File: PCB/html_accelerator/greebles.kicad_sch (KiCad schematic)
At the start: 16 parts, among them U12 MCS9990

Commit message: layout and 3d updates
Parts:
- removed RN1 (x2): 1k, Resistor_SMD:R_Array_Convex_4x1206, symbol Device:R_Pack04
- added MECH1, MECH2: ~, html_accel_footprints:Heatsink, symbol html_accel_Symbols:Heatsink
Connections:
- net GND: now also U12.1 (GND1), U12.10 (PCIE_RXDP), U12.100 (USB0_PWR_EN_N), U12.101 (LN_STAT2), U12.102 (USB1_OVCI_N), U12.103 (USB1_PWR_EN_N), U12.104 (LN_STAT0), U12.105 (LN_STAT1), U12.106 (+3.3VIO), U12.107 (GND20), U12.108 (GND21), U12.109 (+1.2V), U12.11 (GND3), U12.110 (+3.3VA), U12.111 (+3.3VA), U12.112 (USB2_DM), U12.113 (USB2_DP), U12.114 (GND22), U12.115 (GND23), U12.116 (USB2_IBERF), U12.117 (USB2_OTG_VBUS), U12.118 (GND24), U12.119 (+3.3VA), U12.12 (+1.2VA), U12.120 (GND25), U12.121 (+1.2V), U12.122 (USB2_OVCI_N), U12.123 (USB2_PWR_EN_N), U12.124 (USB2_OTG_ID), U12.125 (USB3_OVCI_N), U12.126 (USB3_PWR_EN_N), U12.127 (+3.3VIO), U12.128 (GND26), U12.13 (PCIE_TXDP), U12.14 (PCIE_TXDN), U12.15 (+1.2VA), U12.16 (+3.3VA_PLL), U12.17 (GND4), U12.18 (GND5), U12.19 (+3.3VA_AUX), U12.2 (+3.3VIN_REG), U12.20 (+1.2V), U12.21 (GND6), U12.22 (PCIE_CLKREQ_N), U12.23 (PCIE_WAKE_N), U12.24 (MODE_SEL0), U12.25 (+3.3VIO), U12.26 (GND7), U12.27 (OTG_EN_N), U12.28 (PCIE_PERST_N), U12.29 (EE_SCL), U12.3 (+1.2VOUT_REG), U12.30 (EE_SDA), U12.31 (SCAN_EN), U12.32 (TEST_EN), U12.33 (+1.2V), U12.34 (GND8), U12.35 (GPIO0/D0), U12.36 (GPIO1/D1), U12.37 (GPIO2/D2), U12.38 (GPIO3/D3), U12.39 (GPIO4/D4), U12.4 (PCIE_REFCLKN), U12.40 (GPIO5/D5), U12.41 (GPIO6/D6), U12.42 (GPIO7/D7), U12.43 (GPIO8/INTA), U12.44 (GPIO9/INTB), U12.45 (GPIO10/INTC), U12.46 (GPIO11/INTD), U12.47 (MODE_SEL1), U12.48 (+3.3VIO), U12.49 (MODE_SEL2), U12.5 (PCIE_REFCLKP), U12.50 (GND9), U12.51 (+3.3VA), U12.52 (+3.3VA), U12.53 (USB3_DM), U12.54 (USB3_DP), U12.55 (GND10), U12.56 (GND11), U12.57 (USB3_IBREF), U12.58 (+1.2V), U12.59 (GND12), U12.6 (+1.2VA_AUX), U12.60 (JTAG_TCK), U12.61 (JTAG_TDI), U12.62 (JTAG_TDO), U12.63 (JTAG_TMS), U12.64 (JTAG_TRST_N), U12.65 (GPIO12/CSA_N), U12.66 (GPIO13/CSB_N), U12.67 (GPIO14/CSC_N), U12.68 (GPIO15/CSD_N), U12.69 (GND13), U12.7 (REXT), U12.70 (+3.3VIO), U12.71 (GPIO16/RESET), U12.72 (GPIO17/IOW_N), U12.73 (GPIO18/IOR_N), U12.74 (GPIO23/IOCHRDY2), U12.75 (GPIO19/A0), U12.76 (GPIO20/A1), U12.77 (GPIO21/A2), U12.78 (GPIO22/IOCHRDY1), U12.79 (GND14), U12.8 (GND2), U12.80 (+1.2V), U12.81 (USB0_XSCI), U12.82 (USB0_XSCO), U12.83 (+3.3VA), U12.84 (+3.3VA), U12.85 (USB0_DM), U12.86 (USB0_DP), U12.87 (GND15), U12.88 (GND16), U12.89 (USB0_IBREF), U12.9 (PCIE_RXDN), U12.90 (+3.3VA), U12.91 (+3.3VA), U12.92 (USB1_DM), U12.93 (USB1_DP), U12.94 (GND17), U12.95 (GND18), U12.96 (USB1_IBREF), U12.97 (GND19), U12.98 (+1.2V), U12.99 (USB0_OVCI_N)
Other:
- moved on the sheet: U12A, U12B, U12C, U12D, U12E

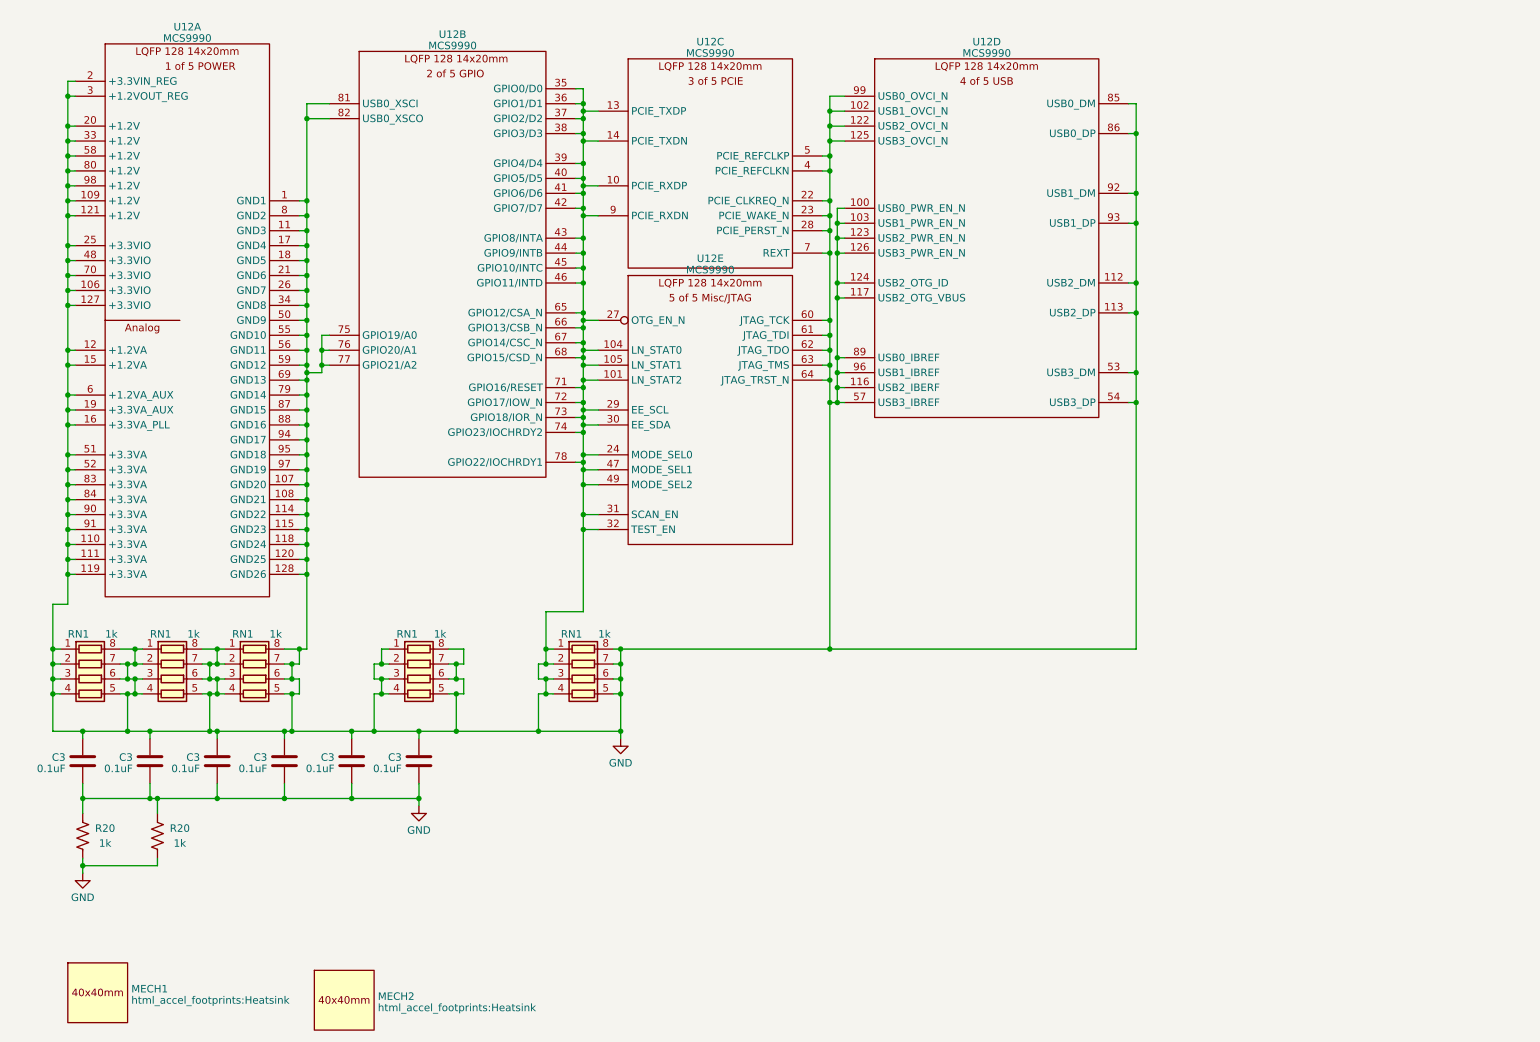
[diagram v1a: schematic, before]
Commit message: constraints for impedance control
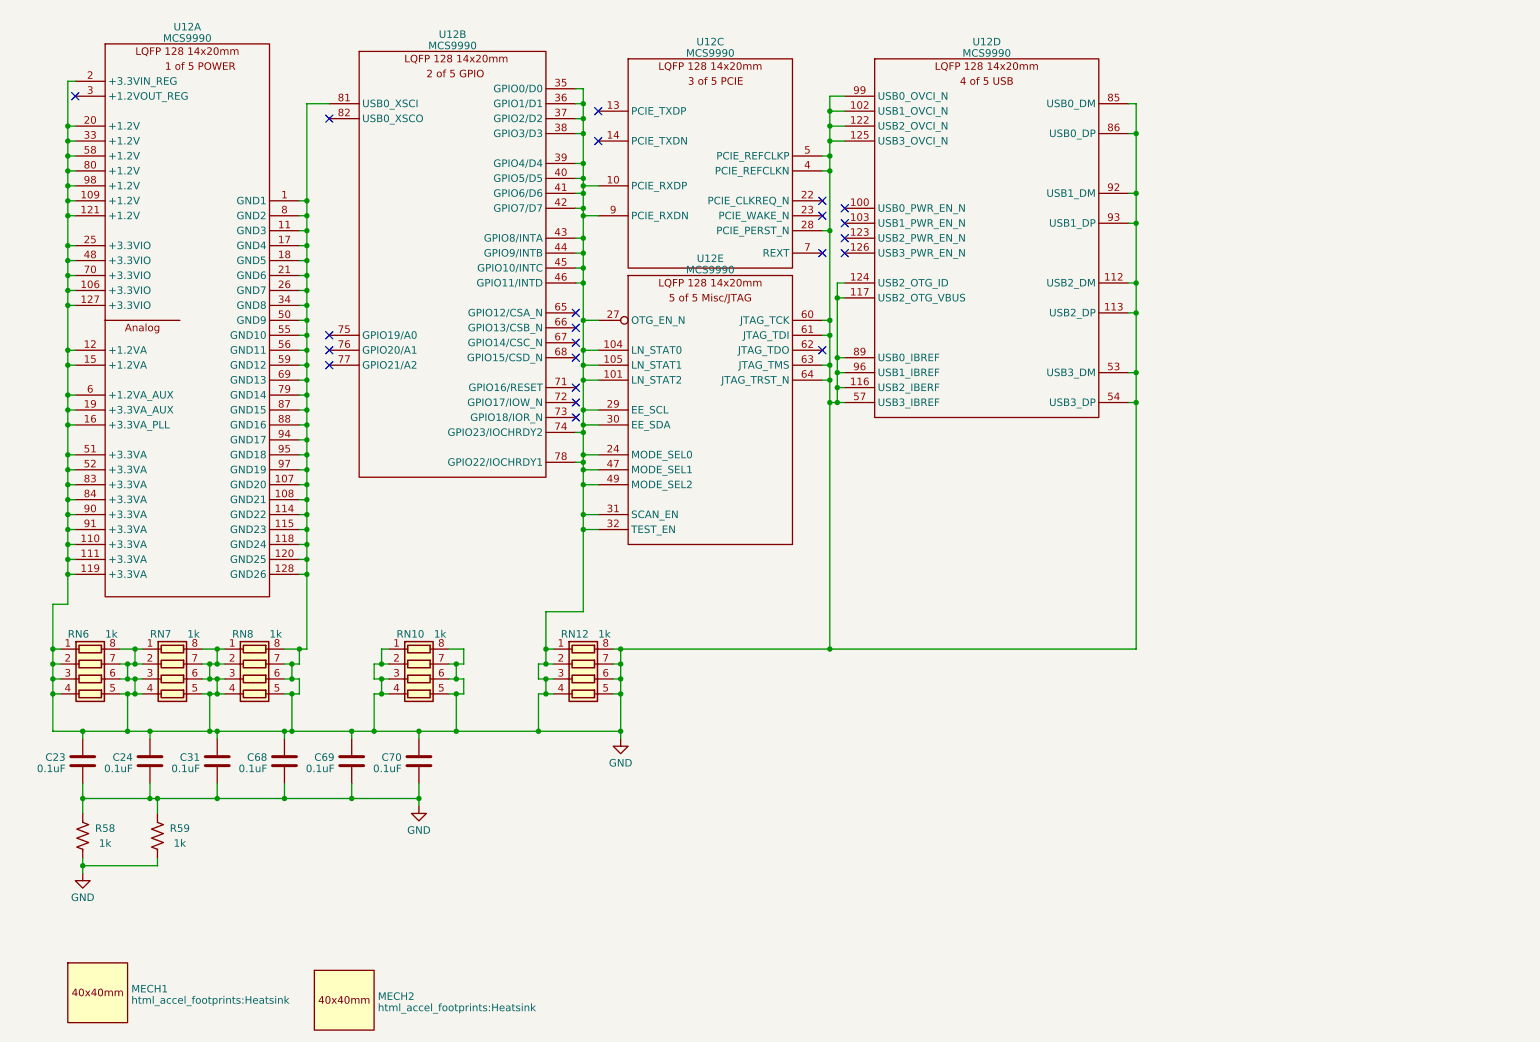
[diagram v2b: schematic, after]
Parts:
- renumbered C3 to C23, C3 to C24, C3 to C31, C3 to C68, C3 to C69, C3 to C70, R20 to R58, R20 to R59, RN1 to RN10, RN1 to RN12, RN1 to RN6, RN1 to RN7, RN1 to RN8
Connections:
- net GND: no longer U12.100 (USB0_PWR_EN_N), U12.103 (USB1_PWR_EN_N), U12.123 (USB2_PWR_EN_N), U12.126 (USB3_PWR_EN_N), U12.13 (PCIE_TXDP), U12.14 (PCIE_TXDN), U12.22 (PCIE_CLKREQ_N), U12.23 (PCIE_WAKE_N), U12.3 (+1.2VOUT_REG), U12.62 (JTAG_TDO), U12.65 (GPIO12/CSA_N), U12.66 (GPIO13/CSB_N), U12.67 (GPIO14/CSC_N), U12.68 (GPIO15/CSD_N), U12.7 (REXT), U12.71 (GPIO16/RESET), U12.72 (GPIO17/IOW_N), U12.73 (GPIO18/IOR_N), U12.75 (GPIO19/A0), U12.76 (GPIO20/A1), U12.77 (GPIO21/A2), U12.82 (USB0_XSCO)
- no-connect marks 0 -> 22

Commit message: Ongoing layout, Update to Kicad V10
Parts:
- MECH1, MECH2: value ~ -> (none)

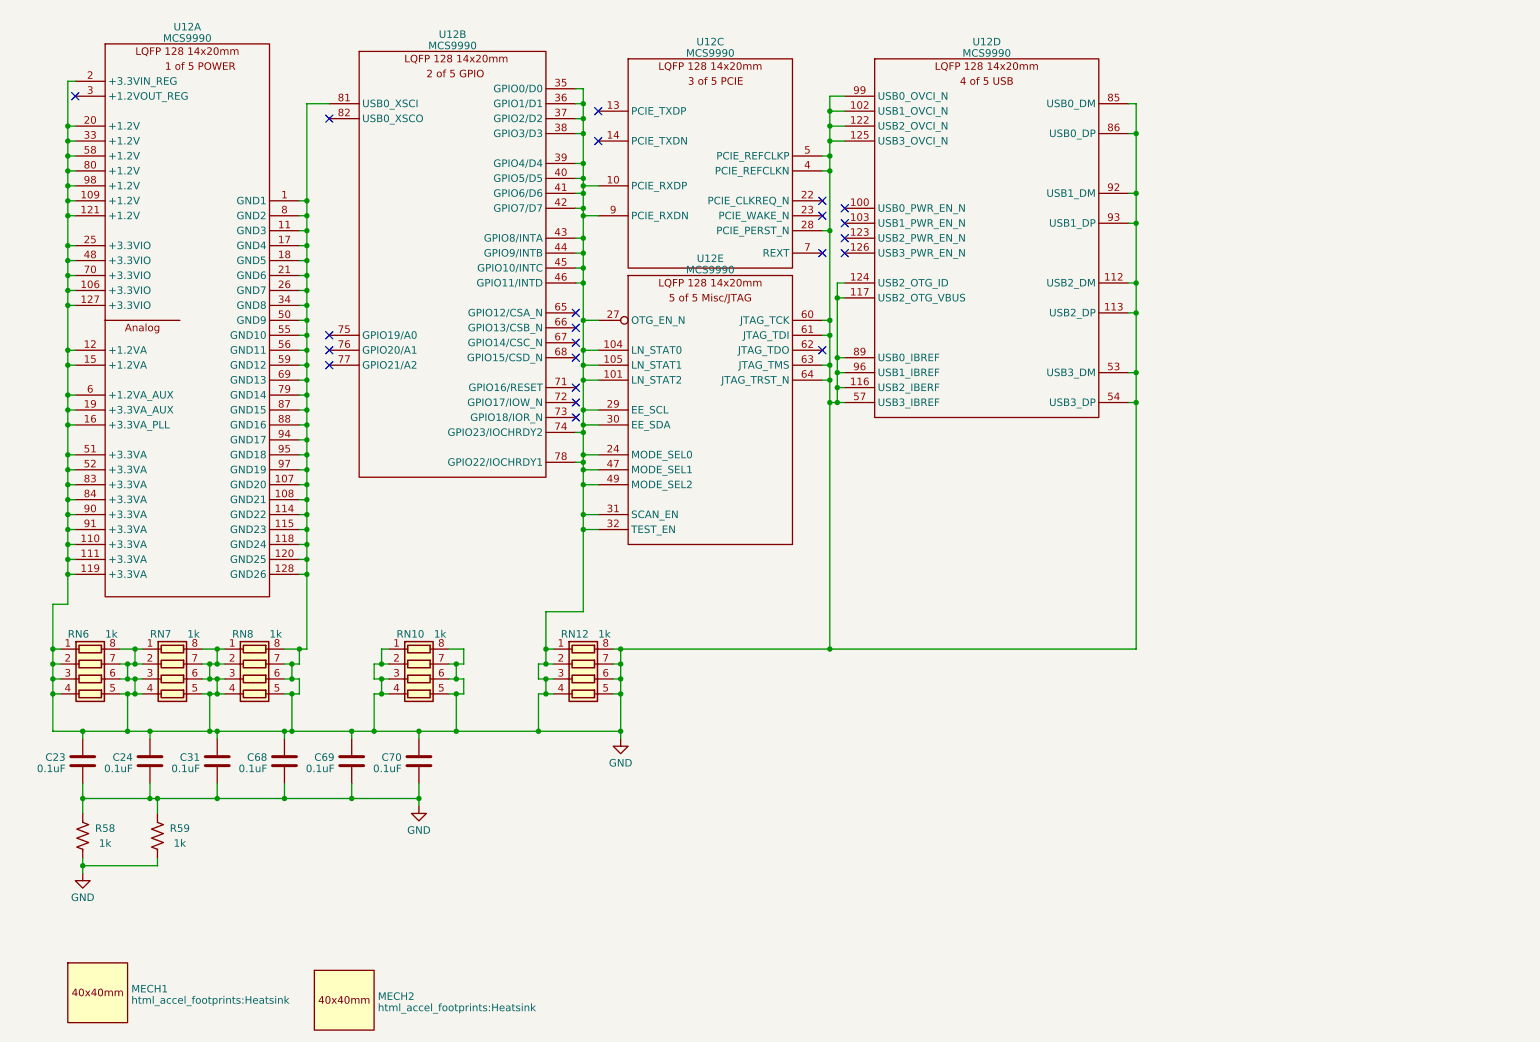
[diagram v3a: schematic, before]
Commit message: Additional routing greebles, cleanup and gerber export with BOM
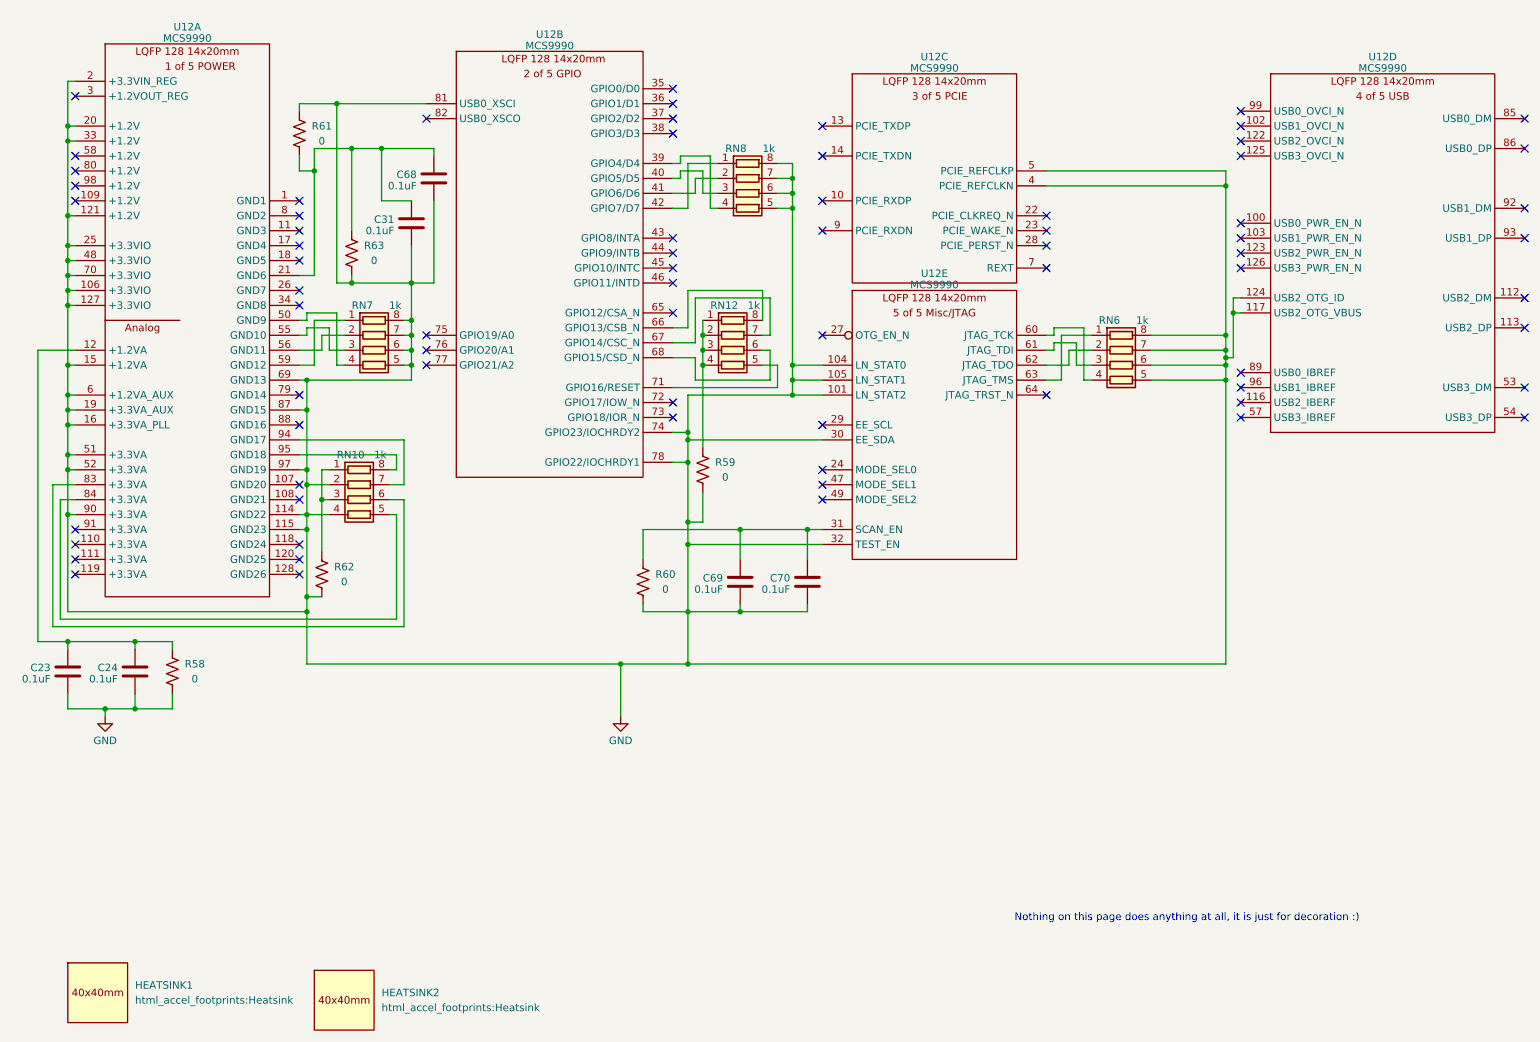
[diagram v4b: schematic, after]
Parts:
- added R60, R61, R62, R63: 0, Resistor_SMD:R_0805_2012Metric_Pad1.20x1.40mm_HandSolder, symbol Device:R_US
- R58, R59: value 1k -> 0
- renumbered MECH1 to HEATSINK1, MECH2 to HEATSINK2
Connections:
- net GND: now also R60.2, R61.1, R62.2, R63.2; no longer C23.2, C24.2, C31.2, C68.2, C69.2, C70.2, R58.1, R59.1, RN10.1 (R1.1), RN10.3 (R3.1), RN10.5 (R4.2), RN10.6 (R3.2), RN10.7 (R2.2), RN10.8 (R1.2), RN12.1 (R1.1), RN12.2 (R2.1), RN12.3 (R3.1), RN12.4 (R4.1), RN12.5 (R4.2), RN12.6 (R3.2), RN12.7 (R2.2), RN12.8 (R1.2), RN6.1 (R1.1), RN6.2 (R2.1), RN6.3 (R3.1), RN6.4 (R4.1), RN7.1 (R1.1), RN7.2 (R2.1), RN7.3 (R3.1), RN7.4 (R4.1), RN8.1 (R1.1), RN8.2 (R2.1), RN8.3 (R3.1), RN8.4 (R4.1), U12.1 (GND1), U12.10 (PCIE_RXDP), U12.102 (USB1_OVCI_N), U12.107 (GND20), U12.108 (GND21), U12.109 (+1.2V), U12.11 (GND3), U12.110 (+3.3VA), U12.111 (+3.3VA), U12.112 (USB2_DM), U12.113 (USB2_DP), U12.116 (USB2_IBERF), U12.118 (GND24), U12.119 (+3.3VA), U12.12 (+1.2VA), U12.120 (GND25), U12.122 (USB2_OVCI_N), U12.125 (USB3_OVCI_N), U12.128 (GND26), U12.17 (GND4), U12.18 (GND5), U12.21 (GND6), U12.24 (MODE_SEL0), U12.26 (GND7), U12.27 (OTG_EN_N), U12.28 (PCIE_PERST_N), U12.29 (EE_SCL), U12.31 (SCAN_EN), U12.34 (GND8), U12.35 (GPIO0/D0), U12.36 (GPIO1/D1), U12.37 (GPIO2/D2), U12.38 (GPIO3/D3), U12.39 (GPIO4/D4), U12.40 (GPIO5/D5), U12.41 (GPIO6/D6), U12.42 (GPIO7/D7), U12.43 (GPIO8/INTA), U12.44 (GPIO9/INTB), U12.45 (GPIO10/INTC), U12.46 (GPIO11/INTD), U12.47 (MODE_SEL1), U12.49 (MODE_SEL2), U12.50 (GND9), U12.53 (USB3_DM), U12.54 (USB3_DP), U12.55 (GND10), U12.56 (GND11), U12.57 (USB3_IBREF), U12.58 (+1.2V), U12.59 (GND12), U12.60 (JTAG_TCK), U12.61 (JTAG_TDI), U12.63 (JTAG_TMS), U12.64 (JTAG_TRST_N), U12.79 (GND14), U12.8 (GND2), U12.80 (+1.2V), U12.83 (+3.3VA), U12.84 (+3.3VA), U12.85 (USB0_DM), U12.86 (USB0_DP), U12.88 (GND16), U12.89 (USB0_IBREF), U12.9 (PCIE_RXDN), U12.91 (+3.3VA), U12.92 (USB1_DM), U12.93 (USB1_DP), U12.94 (GND17), U12.95 (GND18), U12.96 (USB1_IBREF), U12.98 (+1.2V), U12.99 (USB0_OVCI_N)
- net at U12.66 (GPIO13/CSB_N): now also RN12.8 (R1.2)
- net at U12.67 (GPIO14/CSC_N): now also RN12.7 (R2.2)
- net at U12.68 (GPIO15/CSD_N): now also RN12.6 (R3.2)
- net at U12.71 (GPIO16/RESET): now also RN12.5 (R4.2)
- net at U12.62 (JTAG_TDO): now also RN6.2 (R2.1)
- new net: C69.2, C70.2, R60.1, U12.31 (SCAN_EN)
- new net: RN8.4 (R4.1), U12.39 (GPIO4/D4)
- new net: RN8.3 (R3.1), U12.40 (GPIO5/D5)
- new net: RN8.2 (R2.1), U12.41 (GPIO6/D6)
- new net: RN8.1 (R1.1), U12.42 (GPIO7/D7)
- new net: R59.1, RN12.1 (R1.1), RN12.2 (R2.1), RN12.3 (R3.1), RN12.4 (R4.1)
- new net: C23.2, C24.2, R58.1, U12.12 (+1.2VA)
- new net: RN7.1 (R1.1), U12.59 (GND12)
- new net: RN7.2 (R2.1), U12.56 (GND11)
- new net: RN7.3 (R3.1), U12.55 (GND10)
- new net: RN7.4 (R4.1), U12.50 (GND9)
- new net: C31.2, C68.2, R61.2, R63.1, U12.21 (GND6)
- new net: RN10.6 (R3.2), U12.83 (+3.3VA)
- new net: RN10.5 (R4.2), U12.84 (+3.3VA)
- new net: RN10.7 (R2.2), U12.94 (GND17)
- new net: RN10.8 (R1.2), U12.95 (GND18)
- new net: R62.1, RN10.1 (R1.1), RN10.3 (R3.1)
- new net: RN6.4 (R4.1), U12.60 (JTAG_TCK)
- new net: RN6.3 (R3.1), U12.61 (JTAG_TDI)
- new net: RN6.1 (R1.1), U12.63 (JTAG_TMS)
- no-connect marks 22 -> 72
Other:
- note added: "Nothing on this page does anything at all, it is just for decoration :)"
- moved on the sheet: C23, C24, C31, C68, C69, C70, R58, R59, RN10, RN12, RN8, U12B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

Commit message: gerbers and readme updates
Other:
- company: (none) -> Spencer K
- title: USB, 5v POWER -> HTML Accelerator
- moved on the sheet: C23, C24, C31, C68, HEATSINK1, HEATSINK2, R59, R60, R61, R62, R63, RN12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
